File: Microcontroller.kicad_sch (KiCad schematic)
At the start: 17 parts, among them J401 USB_B_Micro, J402 SWD, U401 USBLC6-2SC6, U402 STM32F405RGTx, Y401 25Mhz

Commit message: Switch ADC
Switched from the ADS1115 to ADS7924 to get faster sampling time.
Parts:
- added D401: SS54, Diode_SMD:D_SMA, symbol Device:D_Schottky_Small
- renumbered D401 to D402
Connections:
- net VBUS: now also D401.2 (A)
- new net Vin: D401.1 (K)
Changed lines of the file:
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@@
+    (stroke (width 0) (type default) (color 0 0 0 0))
+  )
+  (wire (pts (xy 50.8 48.26) (xy 53.34 48.26))
     (stroke (width 0) (type default) (color 0 0 0 0))
   )
@@
     (stroke (width 0) (type default) (color 0 0 0 0))
   )
+  (wire (pts (xy 43.18 45.72) (xy 43.18 48.26))
+    (stroke (width 0) (type default) (color 0 0 0 0))
+  )
   (wire (pts (xy 198.12 96.52) (xy 205.74 96.52))
     (stroke (width 0) (type default) (color 0 0 0 0))
@@
     (stroke (width 0) (type default) (color 0 0 0 0))
   )
+  (wire (pts (xy 43.18 48.26) (xy 45.72 48.26))
+    (stroke (width 0) (type default) (color 0 0 0 0))
+  )
   (wire (pts (xy 177.8 147.32) (xy 177.8 149.86))
     (stroke (width 0) (type default) (color 0 0 0 0))
@@
   )
   (wire (pts (xy 154.94 81.28) (xy 154.94 83.82))
+    (stroke (width 0) (type default) (color 0 0 0 0))
+  )
+  (wire (pts (xy 53.34 45.72) (xy 53.34 48.26))
     (stroke (width 0) (type default) (color 0 0 0 0))
   )
@@
   (symbol (lib_id "power:VBUS") (at 68.326 45.974 0) (unit 1)
     (in_bom yes) (on_board yes) (fields_autoplaced)
-    (property "Reference" "#PWR0406" (id 0) (at 68.326 49.784 0)
+    (property "Reference" "#PWR0408" (id 0) (at 68.326 49.784 0)
       (effects (font (size 1.27 1.27)) hide)
     )
@@
   (symbol (lib_id "power:GND") (at 254 60.96 0) (unit 1)
     (in_bom yes) (on_board yes) (fields_autoplaced)
-    (property "Reference" "#PWR0417" (id 0) (at 254 67.31 0)
+    (property "Reference" "#PWR0419" (id 0) (at 254 67.31 0)
       (effects (font (size 1.27 1.27)) hide)
     )
@@
   (symbol (lib_id "power:GND") (at 154.94 83.82 0) (unit 1)
     (in_bom yes) (on_board yes) (fields_autoplaced)
-    (property "Reference" "#PWR0414" (id 0) (at 154.94 90.17 0)
+    (property "Reference" "#PWR0416" (id 0) (at 154.94 90.17 0)
       (effects (font (size 1.27 1.27)) hide)
     )
@@
   (symbol (lib_id "power:GND") (at 134.62 127 0) (unit 1)
     (in_bom yes) (on_board yes) (fields_autoplaced)
-    (property "Reference" "#PWR0411" (id 0) (at 134.62 133.35 0)
+    (property "Reference" "#PWR0413" (id 0) (at 134.62 133.35 0)
       (effects (font (size 1.27 1.27)) hide)
     )
@@
     (pin "2")
   )
+  (symbol (lib_id "power:Vin") (at 53.34 45.72 0) (unit 1)
+    (in_bom yes) (on_board yes) (fields_autoplaced)
+    (property "Reference" "#PWR0105" (id 0) (at 53.34 49.53 0)
+      (effects (font (size 1.27 1.27)) hide)
+    )
+    (property "Value" "Vin" (id 1) (at 53.34 42.1442 0))
+    (property "Footprint" "" (id 2) (at 53.34 45.72 0)
+      (effects (font (size 1.27 1.27)) hide)
+    )
+    (property "Datasheet" "" (id 3) (at 53.34 45.72 0)
+      (effects (font (size 1.27 1.27)) hide)
+    )
+    (pin "1")
+  )
   (symbol (lib_id "power:+3.3V") (at 30.48 114.3 0) (unit 1)
     (in_bom yes) (on_board yes) (fields_autoplaced)
@@
   (symbol (lib_id "power:GND") (at 177.8 149.86 0) (unit 1)
     (in_bom yes) (on_board yes) (fields_autoplaced)
-    (property "Reference" "#PWR0416" (id 0) (at 177.8 156.21 0)
+    (property "Reference" "#PWR0418" (id 0) (at 177.8 156.21 0)
       (effects (font (size 1.27 1.27)) hide)
     )
@@
     )
     (pin "1")
+  )
+  (symbol (lib_id "Device:D_Schottky_Small") (at 48.26 48.26 180) (unit 1)
+    (in_bom yes) (on_board yes) (fields_autoplaced)
+    (property "Reference" "D401" (id 0) (at 48.514 43.5442 0))
+    (property "Value" "SS54" (id 1) (at 48.514 46.0811 0))
+    (property "Footprint" "Diode_SMD:D_SMA" (id 2) (at 48.26 48.26 90)
+      (effects (font (size 1.27 1.27)) hide)
+    )
+    (property "Datasheet" "~" (id 3) (at 48.26 48.26 90)
+      (effects (font (size 1.27 1.27)) hide)
+    )
+    (property "LCSC" "C22452" (id 4) (at 48.26 48.26 0)
+      (effects (font (size 1.27 1.27)) hide)
+    )
+    (pin "1")
+    (pin "2")
   )
   (symbol (lib_id "Connector:USB_B_Micro") (at 25.4 58.42 0) (unit 1)
@@
   (symbol (lib_id "power:+3.3V") (at 175.26 50.8 0) (unit 1)
     (in_bom yes) (on_board yes) (fields_autoplaced)
-    (property "Reference" "#PWR0415" (id 0) (at 175.26 54.61 0)
+    (property "Reference" "#PWR0417" (id 0) (at 175.26 54.61 0)
       (effects (font (size 1.27 1.27)) hide)
     )
@@
   (symbol (lib_id "power:GND") (at 254 144.78 0) (unit 1)
     (in_bom yes) (on_board yes) (fields_autoplaced)
-    (property "Reference" "#PWR0418" (id 0) (at 254 151.13 0)
+    (property "Reference" "#PWR0420" (id 0) (at 254 151.13 0)
       (effects (font (size 1.27 1.27)) hide)
     )
@@
   (symbol (lib_id "Device:LED_Small") (at 254 132.08 90) (unit 1)
     (in_bom yes) (on_board yes) (fields_autoplaced)
-    (property "Reference" "D401" (id 0) (at 255.778 131.1818 90)
+    (property "Reference" "D402" (id 0) (at 255.778 131.1818 90)
       (effects (font (size 1.27 1.27)) (justify right))
     )
@@
   (symbol (lib_id "power:GND") (at 132.08 109.22 0) (unit 1)
     (in_bom yes) (on_board yes) (fields_autoplaced)
-    (property "Reference" "#PWR0410" (id 0) (at 132.08 115.57 0)
+    (property "Reference" "#PWR0412" (id 0) (at 132.08 115.57 0)
       (effects (font (size 1.27 1.27)) hide)
     )
@@
   (symbol (lib_id "power:GND") (at 147.32 83.82 0) (unit 1)
     (in_bom yes) (on_board yes) (fields_autoplaced)
-    (property "Reference" "#PWR0413" (id 0) (at 147.32 90.17 0)
+    (property "Reference" "#PWR0415" (id 0) (at 147.32 90.17 0)
       (effects (font (size 1.27 1.27)) hide)
     )
@@
   (symbol (lib_id "power:GND") (at 127 124.46 0) (unit 1)
     (in_bom yes) (on_board yes) (fields_autoplaced)
-    (property "Reference" "#PWR0409" (id 0) (at 127 130.81 0)
+    (property "Reference" "#PWR0411" (id 0) (at 127 130.81 0)
       (effects (font (size 1.27 1.27)) hide)
     )
@@
     (pin "5")
     (pin "6")
+  )
+  (symbol (lib_id "power:VBUS") (at 43.18 45.72 0) (unit 1)
+    (in_bom yes) (on_board yes) (fields_autoplaced)
+    (property "Reference" "#PWR0406" (id 0) (at 43.18 49.53 0)
+      (effects (font (size 1.27 1.27)) hide)
+    )
+    (property "Value" "VBUS" (id 1) (at 43.18 42.1442 0))
+    (property "Footprint" "" (id 2) (at 43.18 45.72 0)
+      (effects (font (size 1.27 1.27)) hide)
+    )
+    (property "Datasheet" "" (id 3) (at 43.18 45.72 0)
+      (effects (font (size 1.27 1.27)) hide)
+    )
+    (pin "1")
   )
   (symbol (lib_id "Device:Crystal_GND24") (at 127 116.84 0) (unit 1)
@@
   (symbol (lib_id "power:GND") (at 142.24 68.58 0) (unit 1)
     (in_bom yes) (on_board yes) (fields_autoplaced)
-    (property "Reference" "#PWR0412" (id 0) (at 142.24 74.93 0)
+    (property "Reference" "#PWR0414" (id 0) (at 142.24 74.93 0)
       (effects (font (size 1.27 1.27)) hide)
     )
@@
   (symbol (lib_id "power:GND") (at 68.326 71.374 0) (unit 1)
     (in_bom yes) (on_board yes) (fields_autoplaced)
-    (property "Reference" "#PWR0407" (id 0) (at 68.326 77.724 0)
+    (property "Reference" "#PWR0409" (id 0) (at 68.326 77.724 0)
       (effects (font (size 1.27 1.27)) hide)
     )
@@
   (symbol (lib_id "power:GND") (at 119.38 127 0) (unit 1)
     (in_bom yes) (on_board yes) (fields_autoplaced)
-    (property "Reference" "#PWR0408" (id 0) (at 119.38 133.35 0)
-      (effects (font (size 1.27 1.27)) hide)
-    )
+    (property "Reference" "#PWR0410" (id 0) (at 119.38 133.35 0)
+      (effects (font (size 1.27 1.27)) hide)
+    )

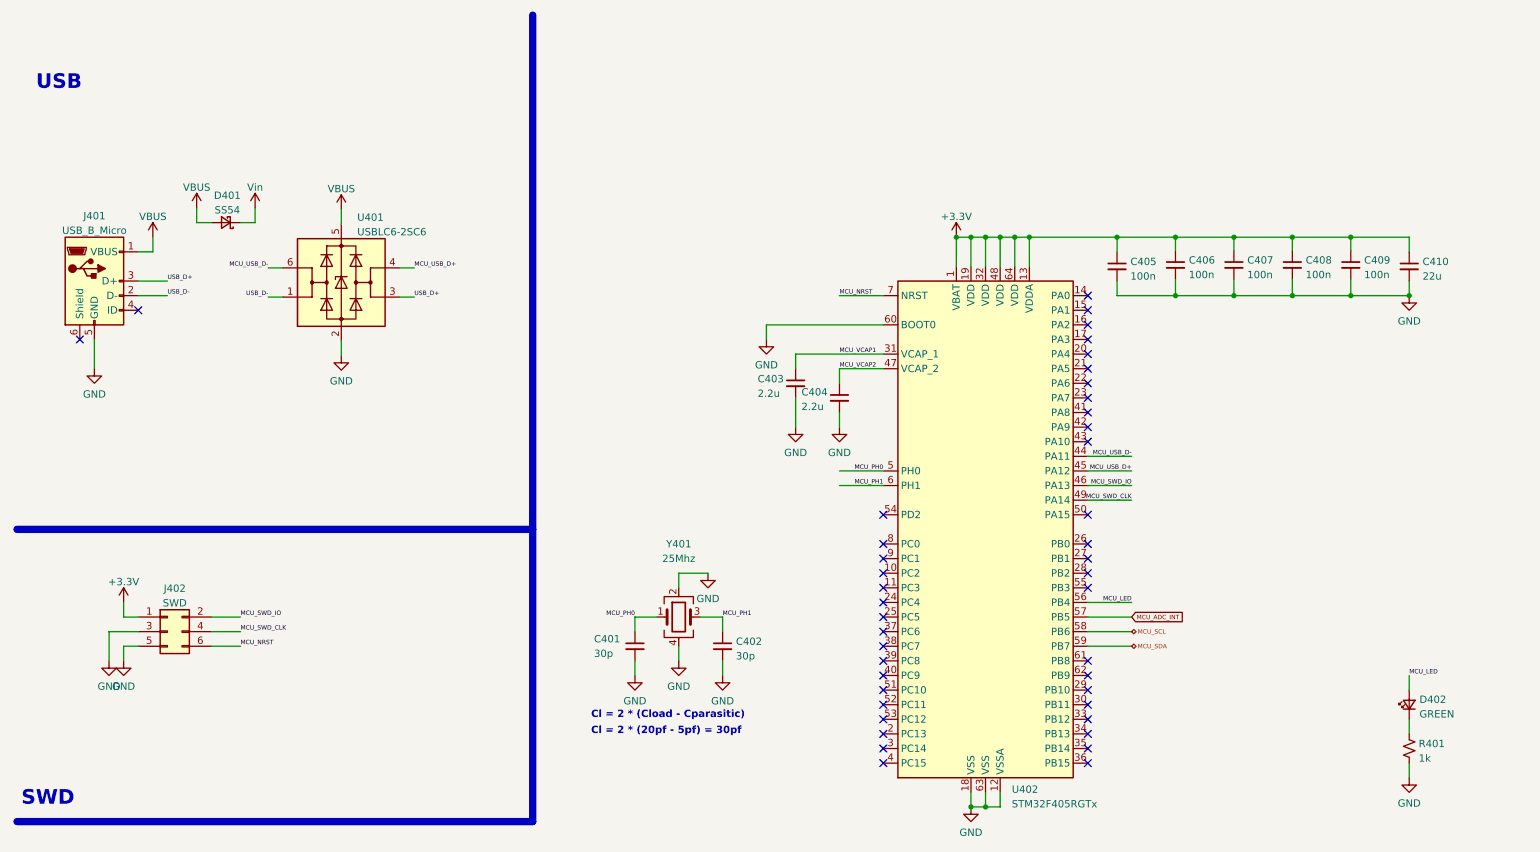
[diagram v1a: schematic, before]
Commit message: Improvements
Switched ADC to ADC128S.
Upgraded USB to USB-C
Improved Analog front end to work with signals better.
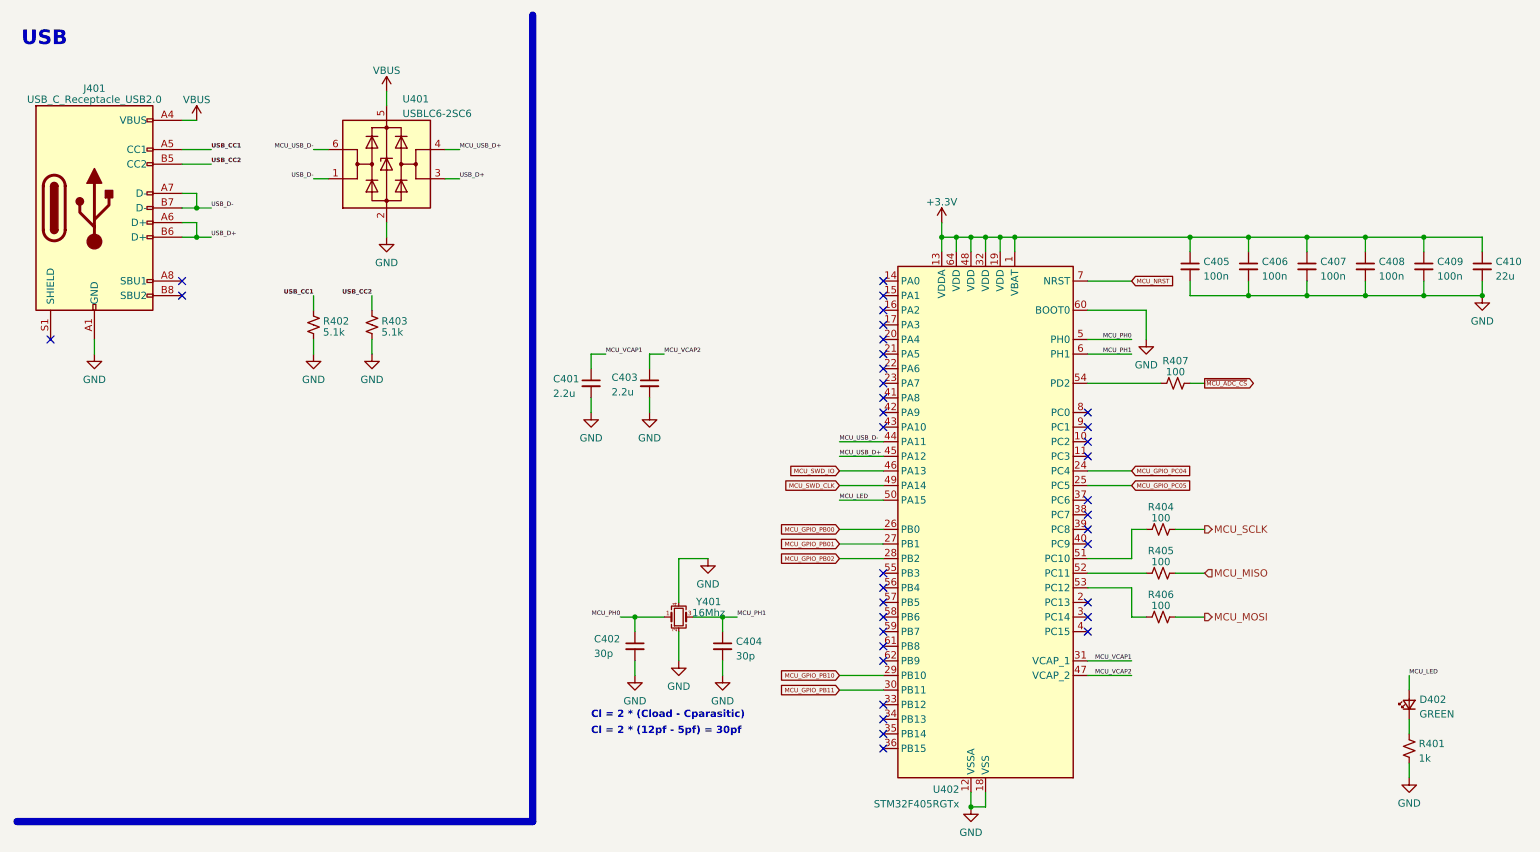
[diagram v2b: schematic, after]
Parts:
- removed D401: SS54, Diode_SMD:D_SMA, symbol Device:D_Schottky_Small
- removed J401: USB_B_Micro, Connector_USB:USB_Micro-B_Amphenol_10104110_Horizontal, symbol Connector:USB_B_Micro
- removed J402: SWD, Connector_PinHeader_2.54mm:PinHeader_2x03_P2.54mm_Vertical, symbol Connector_Generic:Conn_02x03_Odd_Even
- removed Y401: 25Mhz, Crystal:Crystal_SMD_3225-4Pin_3.2x2.5mm, symbol Device:Crystal_GND24
- added J401: USB_C_Receptacle_USB2.0, Connector_USB:USB_C_Receptacle_G-Switch_GT-USB-7010ASV, symbol Connector:USB_C_Receptacle_USB2.0
- added R402, R403: 5.1k, Resistor_SMD:R_0603_1608Metric, symbol Device:R_Small_US
- added R404, R405, R406, R407: 100, Resistor_SMD:R_0603_1608Metric, symbol Device:R_Small_US
- added Y401: 16Mhz, Crystal:Crystal_SMD_3225-4Pin_3.2x2.5mm, symbol Device:Crystal_GND24_Small
- C405, C406, C407, C408, C409: LCSC C57112 -> C105907
- renumbered C403 to C401, C401 to C402, C404 to C403, C402 to C404
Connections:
- net GND: now also J401.A1 (GND), J401.A12 (GND), J401.B1 (GND), J401.B12 (GND), R402.2, R403.2, Y401.2, Y401.4
- net MCU_LED: now also U402.50 (PA15); no longer U402.56 (PB4)
- net MCU_PH0: now also Y401.1
- net MCU_PH1: now also Y401.3
- net USB_D+: now also J401.A6 (D+), J401.B6 (D+)
- net USB_D-: now also J401.A7 (D-), J401.B7 (D-)
- net VBUS: now also J401.A4 (VBUS), J401.A9 (VBUS), J401.B4 (VBUS), J401.B9 (VBUS)
- net MCU_GPIO_PC04: now reaches U402.24 (PC4)
- net MCU_GPIO_PC05: now reaches U402.25 (PC5)
- net MCU_GPIO_PB00: now reaches U402.26 (PB0)
- net MCU_GPIO_PB01: now reaches U402.27 (PB1)
- net MCU_GPIO_PB02: now reaches U402.28 (PB2)
- net MCU_GPIO_PB10: now reaches U402.29 (PB10)
- net MCU_GPIO_PB11: now reaches U402.30 (PB11)
- net at U402.51 (PC10): now also R404.1
- net at U402.52 (PC11): now also R405.1
- net at U402.53 (PC12): now also R406.1
- net at U402.54 (PD2): now also R407.1
- net MCU_ADC_INT: no longer names the net of U402.57 (PB5)
- net MCU_SCL: no longer names the net of U402.58 (PB6)
- net MCU_SDA: no longer names the net of U402.59 (PB7)
- new net MCU_MISO: R405.2
- new net MCU_MOSI: R406.2
- new net MCU_SCLK: R404.2
- new net USB_CC1: J401.A5 (CC1), R402.1
- new net USB_CC2: J401.B5 (CC2), R403.1
- new net ~{MCU_ADC_CS}: R407.2
- no-connect marks 43 -> 36
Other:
- note added: "Cl = 2 * (12pf - 5pf) = 30pf"
- note removed: "Cl = 2 * (20pf - 5pf) = 30pf"
- note removed: "SWD"
- moved on the sheet: C401, C403, C405, C406, C407, C408, C409, C410, U401
